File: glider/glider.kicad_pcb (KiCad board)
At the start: 4 copper layers, 40 x 60 mm, 111 parts, among them J1 SENSOR_I2C, J10 DM3CS-SF, J11 SCH1, J12 IO, J13 SCH2, J14 SCH3, J15 SCH4, J16 SCH5, J17 SCH6, J18 SCH7, J2 USB_B_Micro, J20 CELL, J4 DEBUG_NAV, J6 SCH8, J7 GPS_UART, J8 NCP_COM, J9 IMU_SPI, Q1 DMP1045UQ, Q2 2N7002E, Q3 2N7002E, SW1 NAV_NRST, SW2 NAV_BOOT, U10 MIC5501-3.0YM5, U11 NTB0104, U12 RT6218A, U2 STM32G484RETx, U3 MIC5504-1.8YM5, U4 MCP73831-2-OT, U5 MS5637, U6 W25N01GVZEIG, U7 ICM-20948, U8 L96-M33, Y1 8MHz

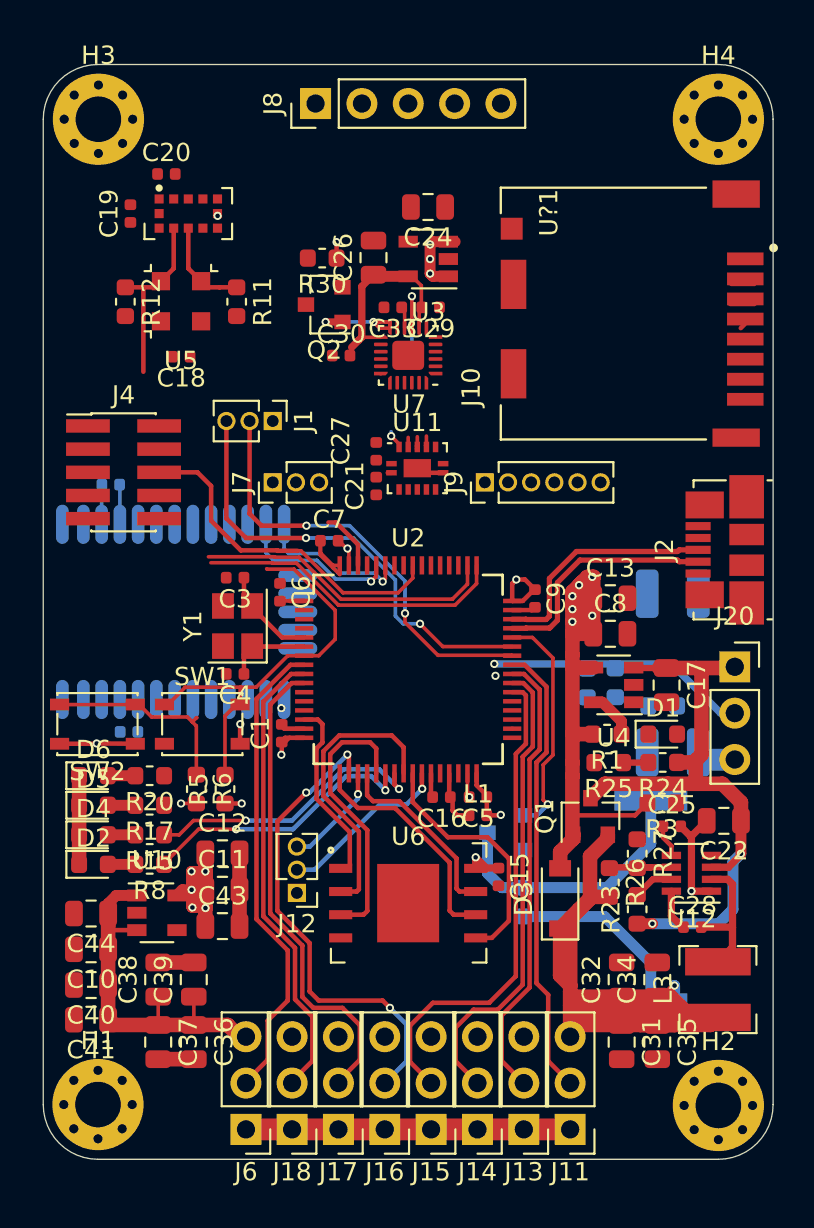
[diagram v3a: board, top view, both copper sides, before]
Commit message: reved layout complete, silkscreen todo
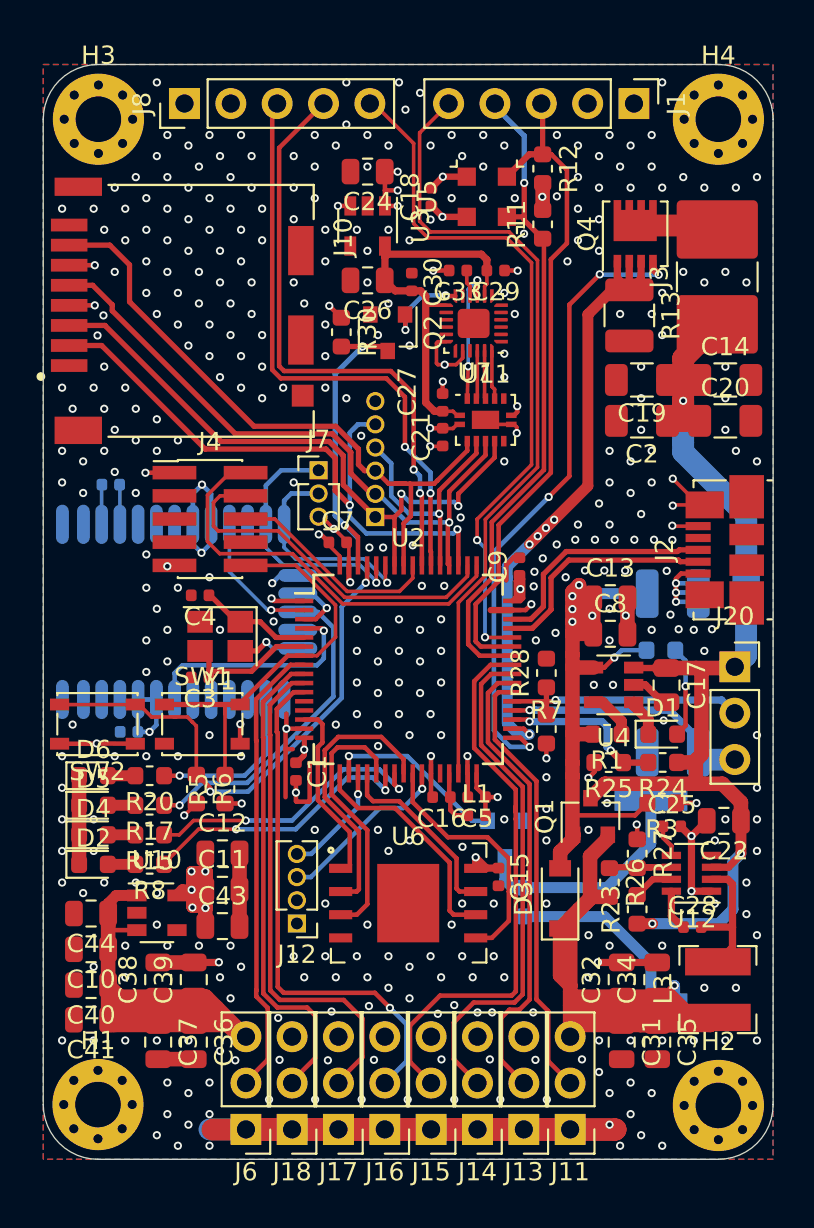
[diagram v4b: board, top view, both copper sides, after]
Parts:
- removed C6: 0.1u, Capacitor_SMD:C_0402_1005Metric
- removed U?1: VL53L1CXV0FY, atlas:LGA-12-3.7x2.1mm
- added C14: 10u, Capacitor_SMD:C_1206_3216Metric, F.Cu at (77.4, 127.3)
- added C2: 10u, Capacitor_SMD:C_1206_3216Metric, F.Cu at (72.8, 129.5)
- added J3: HPS_A, Resistor_SMD:R_2816_7142Metric_Pad3.20x4.45mm_HandSolder, F.Cu at (76.9, 121.6)
- added JP2: HPS_CELL_V, Jumper:SolderJumper-2_P1.3mm_Open_TrianglePad1.0x1.5mm, B.Cu at (78.5, 139.1)
- added Q4: DMT6008LFG, atlas:Diodes_PowerDI3333-8, F.Cu at (72.4, 119.3)
- added R13: 0.1, Resistor_SMD:R_1210_3225Metric, F.Cu at (72.1, 123.8)
- C19, C20: value 0.1u -> 10u; footprint Capacitor_SMD:C_0402_1005Metric -> Capacitor_SMD:C_1206_3216Metric
- J1: footprint Connector_PinHeader_1.27mm:PinHeader_1x03_P1.27mm_Vertical -> Connector_PinHeader_2.54mm:PinHeader_1x05_P2.54mm_Vertical
- J12: footprint Connector_PinHeader_1.27mm:PinHeader_1x03_P1.27mm_Vertical -> Connector_PinHeader_1.27mm:PinHeader_1x04_P1.27mm_Vertical
- J9: moved to B.Cu
- R28, R7: moved to F.Cu
- moved C20 33.5 mm to (77.4, 129.5)
- moved C19 29.5 mm to (72.8, 127.3), turned to 180 degrees
- moved J1 26.4 mm to (72.4, 112.1)
- moved J10 24.4 mm to (47.8, 123.3), turned to 270 degrees
- moved R12 24.0 mm to (67.4, 115.7)
- moved U5 17.7 mm to (64.3, 117.2), turned to 90 degrees
- moved R11 17.3 mm to (67.4, 118.8), turned to 90 degrees
- moved C18 16.3 mm to (61.3, 117.3), turned to 90 degrees
- moved J8 7.18 mm to (47.7, 112.1)
- moved J9 6.29 mm to (58.2, 134.8), turned to 0 degrees
- moved C3 5.79 mm to (48.6, 143.6)
- moved C30 5.59 mm to (60.2, 121.9), turned to 270 degrees
- moved J4 5.39 mm to (49.1, 134.9)
- moved C4 4.72 mm to (48.6, 139.1)
- moved U11 4.58 mm to (64.2, 129.5)
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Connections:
- C19 pad 1: /VDD_MCU -> Net-(C14-Pad1)
- C20 pad 1: /VDD_MCU -> Net-(C14-Pad1)
- J1 pad 1: GND -> /VDD_MCU
- J1 pad 2: /SENSOR_I2C_SDA -> GND
- J11 pad 2: /IO_TIM8_CH4 -> /IO_TIM8_CH1
- J12 pad 2: /OPAMP3_VINM0 -> GND
- J12 pad 3: /IO_TIM2_CH1 -> /IO_1
- J13 pad 2: /IO_TIM8_CH3 -> /IO_TIM8_CH2
- J14 pad 2: /IO_TIM8_CH2 -> /IO_TIM8_CH3
- J15 pad 2: /IO_TIM8_CH1 -> /IO_TIM8_CH4
- J16 pad 2: /IO_TIM3_CH2 -> /IO_TIM1_CH4
- J20 pad 2: /ADC1_IN1_CELL_TS -> /ADC2_IN15_CELL_TS
- J20 pad 3: /OPAMP3_CELL_IS -> /OPAMP2_CELL_IS
- Q3 pad 1: /BUZZER_TIM2_CH4 -> /BUZZER_TIM3_CH2
- R24 pad 2: /OPAMP5_CELL_VS -> /OPAMP4_CELL_VS
- R25 pad 1: /OPAMP5_CELL_VS -> /OPAMP4_CELL_VS
- R28 pad 1: /ADC1_IN1_CELL_TS -> /ADC2_IN15_CELL_TS
- R4 pad 1: /OPAMP3_CELL_IS -> /OPAMP2_CELL_IS
- R7 pad 2: /ADC1_IN1_CELL_TS -> /ADC2_IN15_CELL_TS
- U2 pad 11: /OPAMP5_CELL_VS -> /IO_TIM1_CH4
- U2 pad 12: /ADC1_IN1_CELL_TS -> /HPS_B_TIM2_CH1
- U2 pad 13: /OPAMP3_CELL_IS -> /HPS_B_OPAMP6_CS
- U2 pad 18: /IO_TIM3_CH2 -> /BUZZER_TIM3_CH2
- U2 pad 19: /IO_TIM2_CH1 -> /IO_0
- U2 pad 2: /GPS_FORCEON -> /GPS_RESET
- U2 pad 26: /OPAMP3_VINM0 -> /IO_1
- U2 pad 3: /GPS_EXTINT -> /GPS_FORCEON
- U2 pad 30: /RADIO_USART3_TX -> /I2C_EXT_INT
- U2 pad 33: /RADIO_USART3_RX -> /HPS_A_TIM3_CH2
- U2 pad 34: /RADIO_SET -> /HPS_A_OPAMP3_CS
- U2 pad 35: Net-(U2-Pad35) -> /OPAMP4_CELL_VS
- U2 pad 36: Net-(U2-Pad36) -> /OPAMP2_CELL_IS
- U2 pad 37: Net-(U2-Pad37) -> /ADC2_IN15_CELL_TS
- U2 pad 4: /GPS_FIX -> /GPS_EXTINT
- U2 pad 44: /BUZZER_TIM2_CH4 -> /RADIO_SET
- U2 pad 5: Net-(C3-Pad1) -> Net-(C4-Pad1)
- U2 pad 54: /IMU_SPI2_MOSI -> /RADIO_USART3_TX
- U2 pad 55: Net-(U2-Pad55) -> /RADIO_USART3_RX
- U2 pad 58: /IMU_INT -> /IMU_SPI2_MOSI
- U2 pad 6: Net-(C4-Pad1) -> Net-(C3-Pad1)
- U2 pad 62: /GPS_RESET -> /IMU_INT
- Y1 pad 2: Net-(C3-Pad1) -> GND
- Y1 pad 3: (no net) -> Net-(C3-Pad1)
- Y1 pad 4: (no net) -> GND
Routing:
- net GND: track 50.3 -> 230.7 mm, vias 6 -> 407
- net /I2C_EXT_INT: track 0.00 -> 44.4 mm
- net /RADIO_SET: track 0.01 -> 38.5 mm, vias 0 -> 2
- net /HPS_A_OPAMP3_CS: track 0.00 -> 36.7 mm, vias 0 -> 5
- net /IMU_SPI2_MISO: track 0.00 -> 35.6 mm
- net /HPS_A_TIM3_CH2: track 0.00 -> 35.1 mm, vias 0 -> 4
- net /IMU_SPI2_SCK: track 0.00 -> 34.8 mm, vias 0 -> 1
- net /SD_NCS: track 1.27 -> 35.6 mm, vias 0 -> 2
- net /IMU_SPI2_MOSI: track 1.32 -> 35.0 mm, vias 0 -> 2
- net /RADIO_USART3_RX: track 0.00 -> 33.0 mm, vias 0 -> 2
- net /RADIO_USART3_TX: track 0.00 -> 32.4 mm, vias 0 -> 2
- net /IO_TIM1_CH4: track 0.00 -> 28.7 mm, vias 0 -> 1
- net /IO_TIM3_CH2: track 26.2 -> 0.00 mm, vias 3 -> 0
- net /VDD_IMU: track 12.2 -> 34.5 mm
- net Net-(C14-Pad1): track 0.00 -> 22.0 mm, vias 0 -> 1
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- added copper zone on In1.Cu, net /VDD_MCU
- added copper zone on B.Cu, net GND
- added copper zone on F.Cu, net GND
- added copper zone on In2.Cu, net GND

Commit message: submitted to jlc
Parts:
- removed the C23 at (44.7, 146.6)
- removed the C25 at (74.5, 151.8)
- removed the C28 at (75.6, 157.3)
- removed the J3 at (76.9, 121.6)
- removed the R15 at (45.8, 152.2)
- removed the R18 at (43.7, 133.0)
- removed the R20 at (45.8, 149.0)
- removed R26: 100k, Resistor_SMD:R_0603_1608Metric
- removed the R8 at (45.8, 153.8)
- added C18: 0.1u, Capacitor_SMD:C_0402_1005Metric, F.Cu at (49.0, 151.2)
- added C21: 0.1u, Capacitor_SMD:C_0402_1005Metric, F.Cu at (43.4, 152.3)
- added C26: 0.1u, Capacitor_SMD:C_0402_1005Metric, B.Cu at (54.1, 121.5)
- added D7: SD1206T040S2R0, Diode_SMD:D_SOD-123, B.Cu at (79.1, 153.7)
- added D8: USB_PWR, LED_SMD:LED_0603_1608Metric, F.Cu at (66.0, 148.8)
- added J1: HPS_A, Resistor_SMD:R_2816_7142Metric_Pad3.20x4.45mm_HandSolder, F.Cu at (79.1, 154.2)
- added JP1: HPS_CELL_V, Jumper:SolderJumper-2_P1.3mm_Open_TrianglePad1.0x1.5mm, B.Cu at (65.1, 155.8)
- added N1: Bottom Graphic, atlas:boardartswift, B.Cu at (60.7, 136.7)
- added R12: 0, Resistor_SMD:R_0402_1005Metric, B.Cu at (67.2, 120.5)
- added R13: 100k, Resistor_SMD:R_0603_1608Metric, F.Cu at (52.5, 150.7)
- added R19: 1k, Resistor_SMD:R_0603_1608Metric, F.Cu at (46.9, 122.7)
- added R21: 1k, Resistor_SMD:R_0603_1608Metric, F.Cu at (48.5, 122.7)
- added R23: 1k, Resistor_SMD:R_0603_1608Metric, F.Cu at (51.7, 122.7)
- added R25: 1k, Resistor_SMD:R_0603_1608Metric, B.Cu at (62.6, 147.6)
- added R9: 100k, Resistor_SMD:R_0603_1608Metric, F.Cu at (45.9, 147.8)
- added TP1: VREFBUF, TestPoint:TestPoint_THTPad_D1.0mm_Drill0.5mm, B.Cu at (54.1, 138.3)
- added TP2: VCC_SYS, TestPoint:TestPoint_THTPad_D1.0mm_Drill0.5mm, B.Cu at (33.0, 125.7)
- added TP3: VDD_MCU, TestPoint:TestPoint_THTPad_D1.0mm_Drill0.5mm, B.Cu at (33.0, 123.6)
- added TP4: VDD_IMU, TestPoint:TestPoint_THTPad_D1.0mm_Drill0.5mm, B.Cu at (74.0, 137.7)
- D2: renamed from D3; value D_Schottky -> SD1206T040S2R0
- J18: renamed from J9; moved to F.Cu
- moved H1 48.2 mm to (33.7, 119.8), turned to 270 degrees
- moved H2 45.3 mm to (33.6, 153.8), turned to 270 degrees
- moved H3 45.2 mm to (87.7, 119.8), turned to 270 degrees
- moved J13 44.6 mm to (32.3, 127.9), turned to 90 degrees
- moved J12 43.5 mm to (32.3, 130.4), turned to 90 degrees
- moved C42 43.2 mm to (38.4, 119.4), turned to 90 degrees
- moved J6 43.0 mm to (32.3, 145.6), turned to 90 degrees
- moved J11 42.7 mm to (32.3, 132.9), turned to 90 degrees
- moved J17 42.6 mm to (88.6, 124.5), turned to 0 degrees
- moved J7 42.4 mm to (32.3, 143.1), turned to 90 degrees
- moved J10 42.2 mm to (32.3, 135.5), turned to 90 degrees
- moved H4 42.1 mm to (87.7, 153.8), turned to 270 degrees
- moved J8 42.0 mm to (32.3, 140.5), turned to 90 degrees
- moved J9 41.9 mm to (32.3, 138.0), turned to 90 degrees
- moved C38 41.6 mm to (37.1, 123.0), turned to 180 degrees
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- renumbered C19 to C1, C20 to C10, C16 to C11, C18 to C12, C24 to C13, C21 to C14, C22 to C15, C8 to C16, C13 to C17, C26 to C19, C1 to C2, C27 to C20, C29 to C22, C30 to C23, C17 to C24, C31 to C25, C32 to C27, C33 to C28, C44 to C29, C4 to C3, C10 to C30, C15 to C31, C11 to C32, C12 to C33, C43 to C34, C34 to C35, C35 to C36, C36 to C37, C37 to C38, C38 to C39, C3 to C4, C39 to C40, C40 to C41, C41 to C42, C2 to C5, C5 to C6, C14 to C8, D2 to D3, J16 to J10, J17 to J11, J18 to J12, J6 to J13, J1 to J14, J12 to J15, J7 to J16, J8 to J17, J4 to J2, J20 to J3, J2 to J4, J10 to J5, J11 to J6, J13 to J7, J14 to J8, J15 to J9, L3 to L2, Q4 to Q1, Q1 to Q2, Q2 to Q3, Q3 to Q4, R13 to R1, R27 to R10, R30 to R11, R25 to R14, R31 to R15, R7 to R16, R28 to R17, R6 to R18, R4 to R2, R5 to R20, R17 to R22, R23 to R3, R1 to R4, R11 to R5, R12 to R6, R2 to R7, R3 to R8, SW2 to SW1, SW1 to SW2, U2 to U1, U6 to U10, U3 to U2, U11 to U3, U5 to U4, U12 to U5, U4 to U6, U10 to U9
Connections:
- net /IMU_SPI2_MISO renamed /IMU_SPI3_MISO
- net /IMU_SPI2_MOSI renamed /IMU_SPI3_MOSI
- net /IMU_SPI2_SCK renamed /IMU_SPI3_SCK
- net Net-(C13-Pad1) renamed /VCC_USB
- R24 pad 1: /CELL_POS -> GND
- R24 pad 2: /OPAMP4_CELL_VS -> /IMU_SPI_LS_EN
- U1 pad 12: /HPS_B_TIM2_CH1 -> /GPS_FIX
- U1 pad 13: /HPS_B_OPAMP6_CS -> /IMU_SPI_LS_EN
- U3 pad 8: /VDD_MCU -> /IMU_SPI_LS_EN
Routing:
- net Net-(C1-Pad1): track 22.0 -> 74.6 mm, vias 1 -> 12
- net Net-(D7-Pad2): track 4.59 -> 41.9 mm, vias 0 -> 9
- net /IMU_SPI_LS_EN: track 0.00 -> 27.0 mm
- net /CELL_POS: track 39.7 -> 61.4 mm
- net /GPS_FIX: track 9.13 -> 15.5 mm, vias 1 -> 2
- net /VDD_SYS: track 148.1 -> 154.2 mm
- net /VDD_IMU: track 34.5 -> 29.4 mm
- net Net-(D8-Pad2): track 0.00 -> 3.68 mm, vias 0 -> 1
- net /VREFBUF_OUT: track 0.00 -> 2.37 mm
- net /HPS_A_OPAMP3_CS: track 36.7 -> 38.9 mm, vias 5 -> 6
- net GND: track 230.7 -> 228.5 mm, vias 407 -> 415
- net /VDD_MCU: track 60.6 -> 59.5 mm, vias 26 -> 23
- net /IMU_INT: track 16.8 -> 15.9 mm
- net /ADC2_IN15_CELL_TS: track 14.8 -> 15.7 mm
- net /VCC_USB: track 36.8 -> 36.0 mm
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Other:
- board size 40 x 60 mm -> 60 x 40 mm
- rule pad_to_mask_clearance: 0 -> 0.05
- rule via_min_size: 0.45 -> 0.4
- board text added: "+"
- board text added: "-"
- board text added: "--"
- board text added: "BOOT ~ RESET"
- board text added: "BUCK"
- board text added: "C"
- board text added: "F"
- board text added: "GPS"
- board text added: "HCS"
- board text added: "I2C"
- board text added: "IMU"
- board text added: "IO"
- board text added: "P"
- board text added: "S"
- board text added: "SD"
- board text added: "SPI"
- board text added: "SWD"
- board text added: "T"
- board text added: "T1C1"
- board text added: "T1C4"
- board text added: "T8C1"
- board text added: "T8C4"
- board text added: "UART"
- board text added: "USB"
- board text added: "W"
